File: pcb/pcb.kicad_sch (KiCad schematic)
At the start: 17 parts, among them CN10 1x2, CN2 1x8, CN3 1x8, CN4 1x8, CN5 1x4, CN6 1x2, CN7 1x2, SW1 switch_3x4, SW2 switch_3x4, SW3 219-3LPST

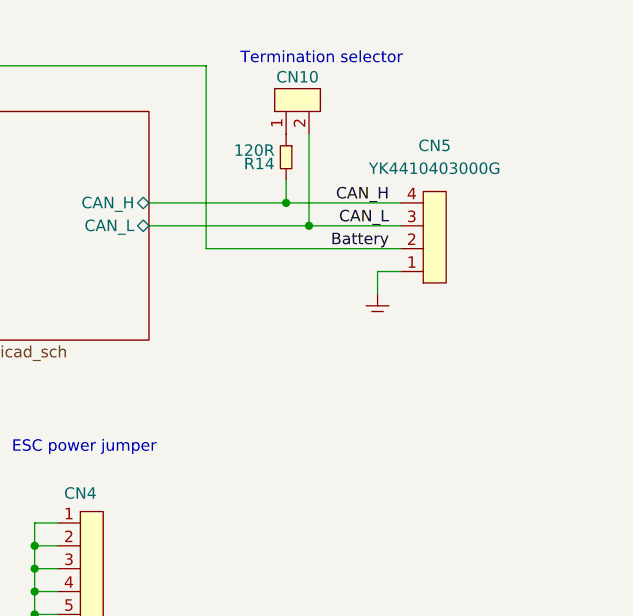
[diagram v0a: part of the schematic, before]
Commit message: changed output connector to xt60 & 2x jst-xh-4
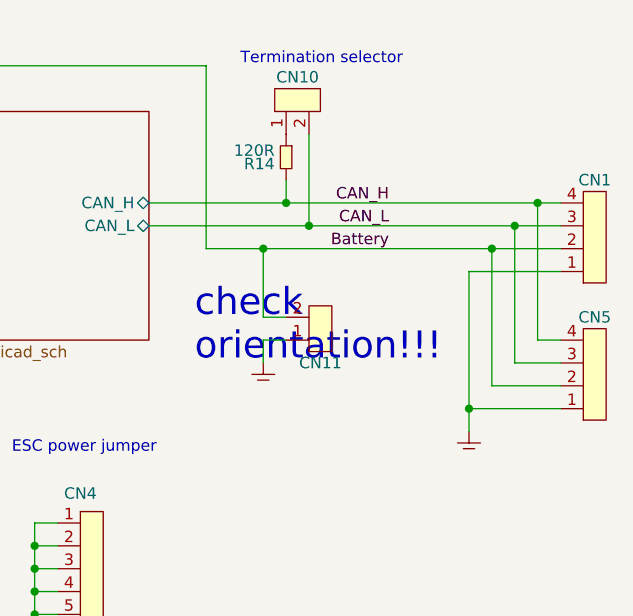
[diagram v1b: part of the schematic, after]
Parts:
- added CN1: 1x4, jst-xh:jst-xh-4, symbol jst-xh:1x4
- added CN11: 1x2, connectors:XT60, symbol pin_headers:1x2
- CN5: footprint connectors:YK4410403000G -> jst-xh:jst-xh-4; symbol pin_headers:1x4 -> jst-xh:1x4; DigiKey (none) -> 455-B4B-XH-A-ND; MPN YK4410403000G -> B4B-XH-A; Manufacturer (none) -> JST
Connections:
- net Battery: now also CN1.2, CN11.2
- net CAN_H: now also CN1.4
- net CAN_L: now also CN1.3
- net GND: now also CN1.1, CN11.1
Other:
- note added: "check orientation!!!"
- moved on the sheet: CN5

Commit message: worked on layout
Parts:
- removed CN8: ~, USB:USB4105-GF-A, symbol connectors:USB4105-GF-A
- removed R12, R13: 5k1, SMT:0603, symbol generic:R
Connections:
- net CAN_H: now also CN10.1; no longer R14.2
- net CAN_L: now also R14.2; no longer CN10.2
- net at R14.1: now also CN10.2; no longer CN10.1
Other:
- sheet MCU ports: added none; removed USB_N, USB_P
- moved on the sheet: R14

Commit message: worked on pinout
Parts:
- removed SW1, SW2: switch_3x4, buttons:sw_3x4, symbol switches:switch_3x4
- added R12: 10K, SMT:0603, symbol generic:R
- added TP1: test_point, PCB:test_point, symbol PCB:test_point
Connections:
- net GND: now also R12.1
- net MCU/DFU: now also R12.2, TP1.1 (TP)
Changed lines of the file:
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@@
     (comment 1 "User interfaces")
   )
-  (junction (at 129.54 121.92) (diameter 0) (color 0 0 0 0)
-  )
   (junction (at 251.46 109.22) (diameter 0) (color 0 0 0 0)
   )
@@
   (junction (at 203.2 132.08) (diameter 0) (color 0 0 0 0)
   )
+  (junction (at 129.54 116.84) (diameter 0) (color 0 0 0 0)
+  )
   (junction (at 129.54 137.16) (diameter 0) (color 0 0 0 0)
   )
   (junction (at 203.2 129.54) (diameter 0) (color 0 0 0 0)
   )
-  (junction (at 129.54 132.08) (diameter 0) (color 0 0 0 0)
-  )
   (junction (at 190.5 124.46) (diameter 0) (color 0 0 0 0)
   )
@@
     (stroke (width 0) (type default))
   )
-  (wire (pts (xy 129.54 116.84) (xy 132.08 116.84))
-    (stroke (width 0) (type default))
-  )
-  (wire (pts (xy 129.54 132.08) (xy 129.54 121.92))
-    (stroke (width 0) (type default))
-  )
   (wire (pts (xy 203.2 137.16) (xy 205.74 137.16))
     (stroke (width 0) (type default))
   )
+  (wire (pts (xy 129.54 116.84) (xy 129.54 119.38))
+    (stroke (width 0) (type default))
+  )
   (wire (pts (xy 203.2 127) (xy 205.74 127))
     (stroke (width 0) (type default))
@@
     (stroke (width 0) (type default))
   )
-  (wire (pts (xy 137.16 116.84) (xy 139.7 116.84))
-    (stroke (width 0) (type default))
-  )
   (wire (pts (xy 137.16 132.08) (xy 139.7 132.08))
     (stroke (width 0) (type default))
@@
     (stroke (width 0) (type default))
   )
+  (wire (pts (xy 139.7 116.84) (xy 129.54 116.84))
+    (stroke (width 0) (type default))
+  )
   (wire (pts (xy 231.14 99.06) (xy 228.6 99.06))
     (stroke (width 0) (type default))
@@
     (stroke (width 0) (type default))
   )
-  (wire (pts (xy 129.54 121.92) (xy 132.08 121.92))
-    (stroke (width 0) (type default))
-  )
   (wire (pts (xy 203.2 127) (xy 203.2 124.46))
     (stroke (width 0) (type default))
   )
-  (wire (pts (xy 137.16 121.92) (xy 139.7 121.92))
-    (stroke (width 0) (type default))
-  )
   (wire (pts (xy 193.04 114.3) (xy 190.5 114.3))
     (stroke (width 0) (type default))
@@
     (stroke (width 0) (type default))
   )
+  (wire (pts (xy 129.54 124.46) (xy 129.54 127))
+    (stroke (width 0) (type default))
+  )
   (wire (pts (xy 233.68 83.82) (xy 233.68 88.9))
     (stroke (width 0) (type default))
@@
   )
   (wire (pts (xy 256.54 88.9) (xy 261.62 88.9))
-    (stroke (width 0) (type default))
-  )
-  (wire (pts (xy 129.54 121.92) (xy 129.54 116.84))
     (stroke (width 0) (type default))
   )
@@
     )
   )
-  (symbol (lib_id "switches:switch_3x4") (at 134.62 116.84 0) (unit 1)
+  (symbol (lib_id "generic:GND") (at 129.54 127 0) (unit 1)
     (in_bom yes) (on_board yes) (dnp no) (fields_autoplaced)
-    (property "Reference" "SW1" (at 134.62 114.3 0)
-      (effects (font (size 1.27 1.27)))
-    )
-    (property "Value" "switch_3x4" (at 134.62 114.3 0)
-      (effects (font (size 1.27 1.27)) hide)
-    )
-    (property "Footprint" "buttons:sw_3x4" (at 134.62 118.11 0)
-      (effects (font (size 1.27 1.27)) hide)
-    )
-    (property "Datasheet" "" (at 134.62 116.84 0)
-      (effects (font (size 1.27 1.27)) hide)
-    )
-    (pin "1")
-    (pin "2")
-    (pin "3")
-    (pin "4")
-    (instances
-      (project "pcb"
-        (path "/6bb3bad6-1a89-4624-b34d-6ddda7dd16d2"
-          (reference "SW1") (unit 1)
+    (property "Reference" "#GND02" (at 133.35 125.73 0)
+      (effects (font (size 1.27 1.27)) hide)
+    )
+    (property "Value" "GND" (at 133.35 127 0)
+      (effects (font (size 1.27 1.27)) hide)
+    )
+    (property "Footprint" "" (at 129.54 127 0)
+      (effects (font (size 1.27 1.27)) hide)
+    )
+    (property "Datasheet" "" (at 129.54 127 0)
+      (effects (font (size 1.27 1.27)) hide)
+    )
+    (pin "~")
+    (instances
+      (project "pcb"
+        (path "/6bb3bad6-1a89-4624-b34d-6ddda7dd16d2"
+          (reference "#GND02") (unit 1)
         )
       )
@@
     )
   )
-  (symbol (lib_id "switches:switch_3x4") (at 134.62 121.92 0) (unit 1)
-    (in_bom yes) (on_board yes) (dnp no)
-    (property "Reference" "SW2" (at 134.62 119.38 0)
-      (effects (font (size 1.27 1.27)))
-    )
-    (property "Value" "switch_3x4" (at 134.62 119.38 0)
-      (effects (font (size 1.27 1.27)) hide)
-    )
-    (property "Footprint" "buttons:sw_3x4" (at 134.62 123.19 0)
-      (effects (font (size 1.27 1.27)) hide)
-    )
-    (property "Datasheet" "" (at 134.62 121.92 0)
-      (effects (font (size 1.27 1.27)) hide)
-    )
-    (pin "1")
-    (pin "2")
-    (pin "3")
-    (pin "4")
-    (instances
-      (project "pcb"
-        (path "/6bb3bad6-1a89-4624-b34d-6ddda7dd16d2/19469851-aeaf-466c-9786-c0d0ae531cf4"
-          (reference "SW2") (unit 1)
-        )
-        (path "/6bb3bad6-1a89-4624-b34d-6ddda7dd16d2"
-          (reference "SW2") (unit 1)
-        )
-      )
-    )
-  )
   (symbol (lib_id "generic:GND") (at 129.54 139.7 0) (unit 1)
     (in_bom yes) (on_board yes) (dnp no) (fields_autoplaced)
@@
     )
   )
+  (symbol (lib_id "PCB:test_point") (at 129.54 116.84 0) (mirror y) (unit 1)
+    (in_bom yes) (on_board yes) (dnp no)
+    (property "Reference" "TP1" (at 127 115.57 0)
+      (effects (font (size 1.27 1.27)) (justify left))
+    )
+    (property "Value" "test_point" (at 129.54 114.3 0)
+      (effects (font (size 1.27 1.27)) hide)
+    )
+    (property "Footprint" "PCB:test_point" (at 127 118.11 0)
+      (effects (font (size 1.27 1.27)) hide)
+    )
+    (property "Datasheet" "" (at 129.54 116.84 0)
+      (effects (font (size 1.27 1.27)) hide)
+    )
+    (pin "1")
+    (instances
+      (project "pcb"
+        (path "/6bb3bad6-1a89-4624-b34d-6ddda7dd16d2"
+          (reference "TP1") (unit 1)
+        )
+      )
+    )
+  )
   (symbol (lib_id "pin_headers:1x2") (at 60.96 78.74 0) (mirror y) (unit 1)
     (in_bom yes) (on_board yes) (dnp no) (fields_autoplaced)
@@
         )
       )
+    )
+  )
+  (symbol (lib_name "R_1") (lib_id "generic:R") (at 129.54 121.92 270) (mirror x) (unit 1)
+    (in_bom yes) (on_board yes) (dnp no)
+    (property "Reference" "R12" (at 128.27 120.65 90)
+      (effects (font (size 1.27 1.27)) (justify right))
+    )
+    (property "Value" "10K" (at 128.27 123.19 90)
+      (effects (font (size 1.27 1.27)) (justify right))
+    )
+    (property "Footprint" "SMT:0603" (at 128.905 124.46 0)
+      (effects (font (size 1.27 1.27)) hide)
+    )
+    (property "Datasheet" "" (at 129.54 121.92 0)
+      (effects (font (size 1.27 1.27)) hide)
+    )
+    (pin "1")
+    (pin "2")
+    (instances
+      (project "pcb"
+        (path "/6bb3bad6-1a89-4624-b34d-6ddda7dd16d2"
+          (reference "R12") (unit 1)
+        )
+      )

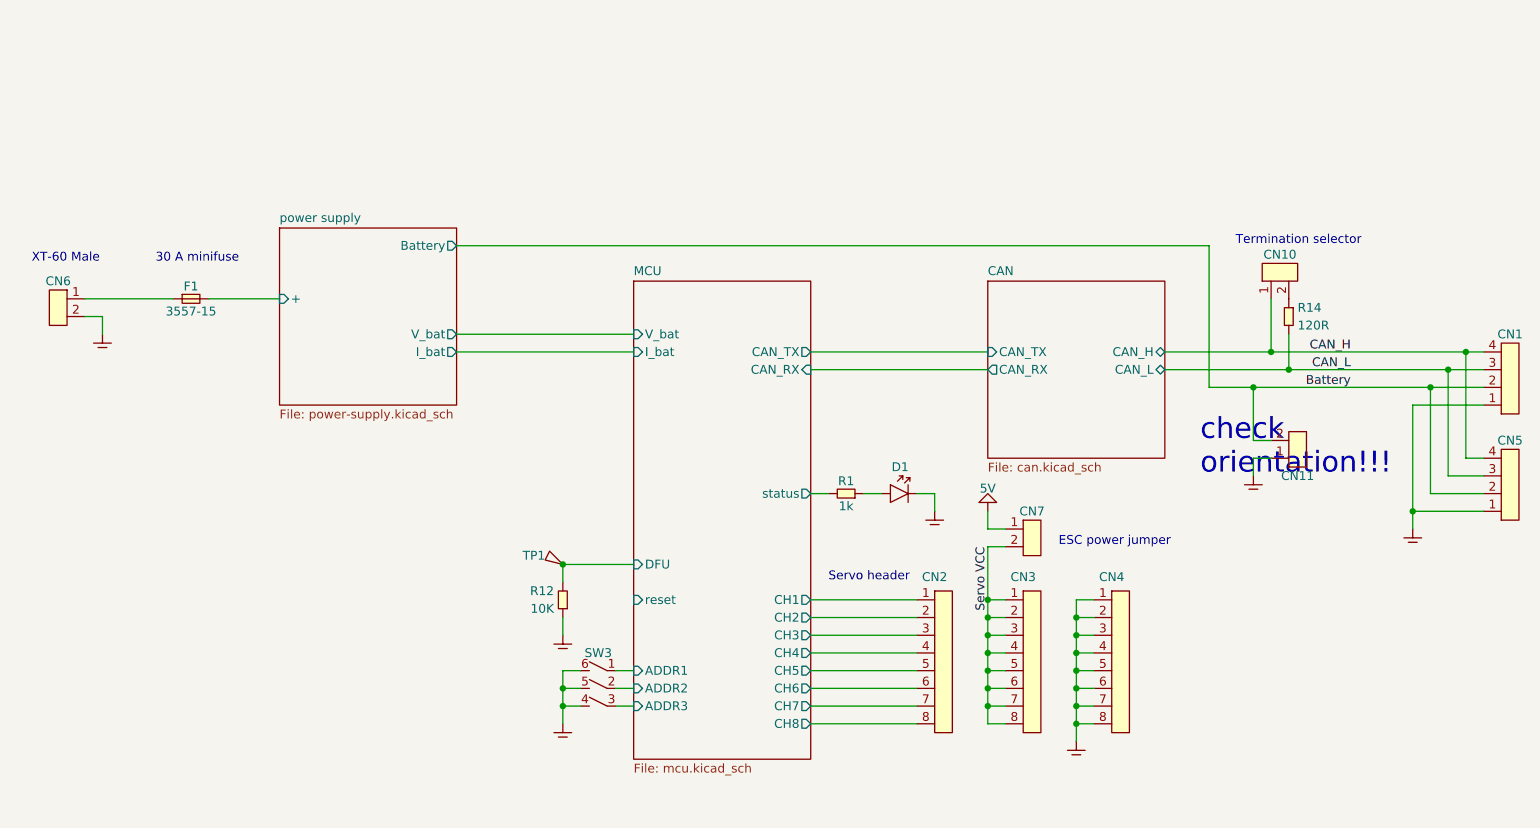
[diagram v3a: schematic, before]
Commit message: added hierarchial sheets for buffering
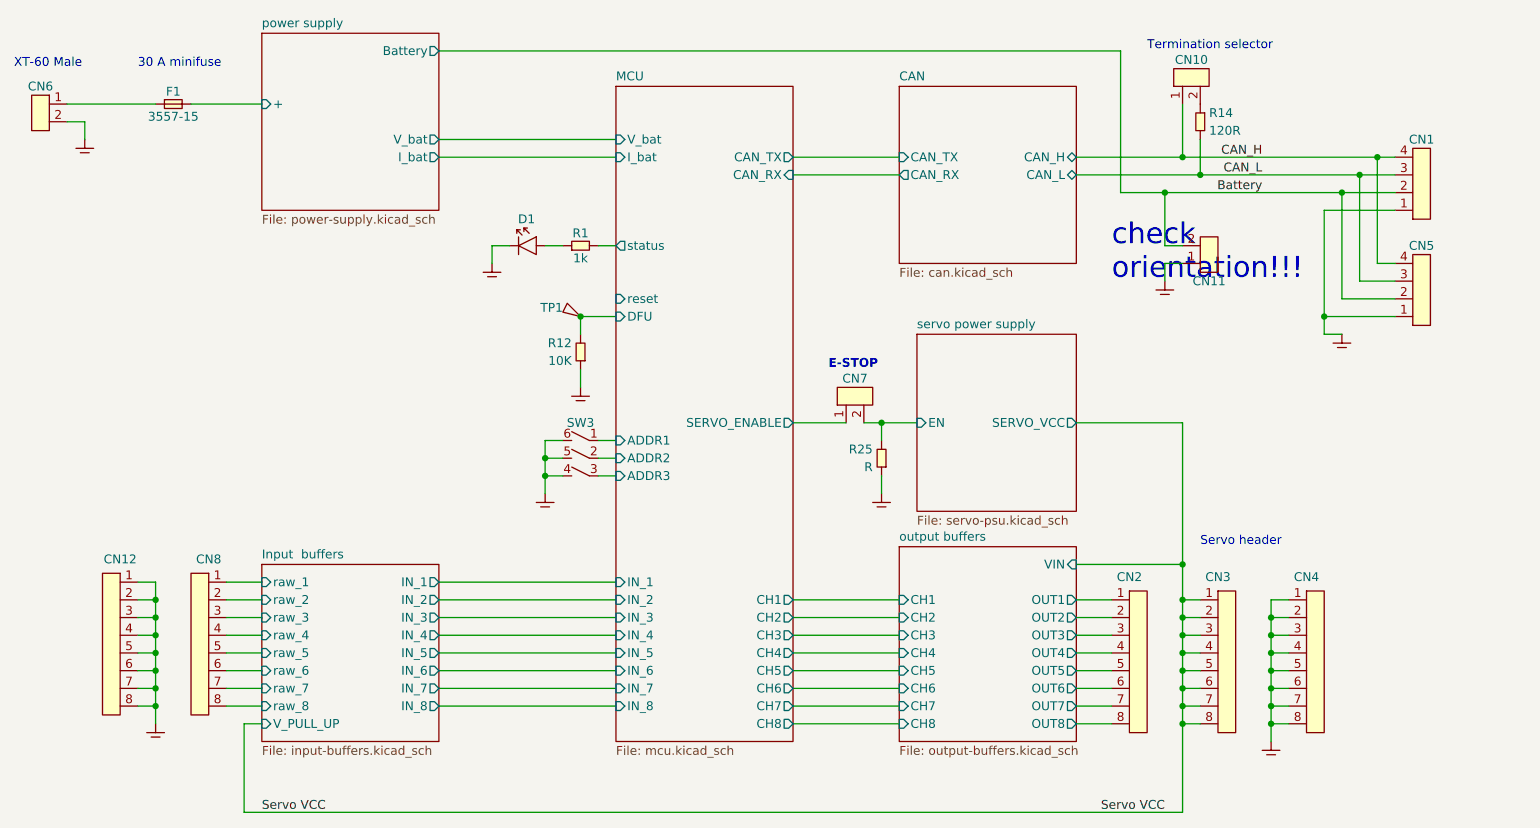
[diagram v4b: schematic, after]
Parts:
- added CN12, CN8: 1x8, pin_headers:1x8, symbol pin_headers:1x8
- added R25: R, SMT:0603, symbol generic:R
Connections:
- net GND: now also CN12.1, CN12.2, CN12.3, CN12.4, CN12.5, CN12.6, CN12.7, CN12.8, R25.1
- net MCU/CH1: no longer CN2.1
- net MCU/CH2: no longer CN2.2
- net MCU/CH3: no longer CN2.3
- net MCU/CH4: no longer CN2.4
- net MCU/CH5: no longer CN2.5
- net MCU/CH6: no longer CN2.6
- net MCU/CH7: no longer CN2.7
- net MCU/CH8: no longer CN2.8
- net Servo VCC: no longer CN7.2
- net 5V renamed MCU/SERVO_ENABLE
- new net Input  buffers/raw_1: CN8.1
- new net Input  buffers/raw_2: CN8.2
- new net Input  buffers/raw_3: CN8.3
- new net Input  buffers/raw_4: CN8.4
- new net Input  buffers/raw_5: CN8.5
- new net Input  buffers/raw_6: CN8.6
- new net Input  buffers/raw_7: CN8.7
- new net Input  buffers/raw_8: CN8.8
- new net output buffers/OUT1: CN2.1
- new net output buffers/OUT2: CN2.2
- new net output buffers/OUT3: CN2.3
- new net output buffers/OUT4: CN2.4
- new net output buffers/OUT5: CN2.5
- new net output buffers/OUT6: CN2.6
- new net output buffers/OUT7: CN2.7
- new net output buffers/OUT8: CN2.8
- new net servo power supply/EN: CN7.2, R25.2
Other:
- added sheet Input  buffers (input-buffers.kicad_sch)
- added sheet output buffers (output-buffers.kicad_sch)
- added sheet servo power supply (servo-psu.kicad_sch)
- sheet MCU ports: added IN_1, IN_2, IN_3, IN_4, IN_5, IN_6, IN_7, IN_8, SERVO_ENABLE; removed none
- note added: "E-STOP"
- note removed: "ESC power jumper"
- moved on the sheet: CN1, CN10, CN11, CN2, CN3, CN4, CN5, CN6, CN7, D1, F1, R1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

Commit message: worked on layout
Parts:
- renumbered R1 to R4
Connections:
- net output buffers/OUT1 renamed output buffers/OUT_1
- net output buffers/OUT2 renamed output buffers/OUT_2
- net output buffers/OUT3 renamed output buffers/OUT_3
- net output buffers/OUT4 renamed output buffers/OUT_4
- net output buffers/OUT5 renamed output buffers/OUT_5
- net output buffers/OUT6 renamed output buffers/OUT_6
- net output buffers/OUT7 renamed output buffers/OUT_7
- net output buffers/OUT8 renamed output buffers/OUT_8
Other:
- sheet output buffers ports: added OUT_1, OUT_2, OUT_3, OUT_4, OUT_5, OUT_6, OUT_7, OUT_8; removed OUT1, OUT2, OUT3, OUT4, OUT5, OUT6, OUT7, OUT8

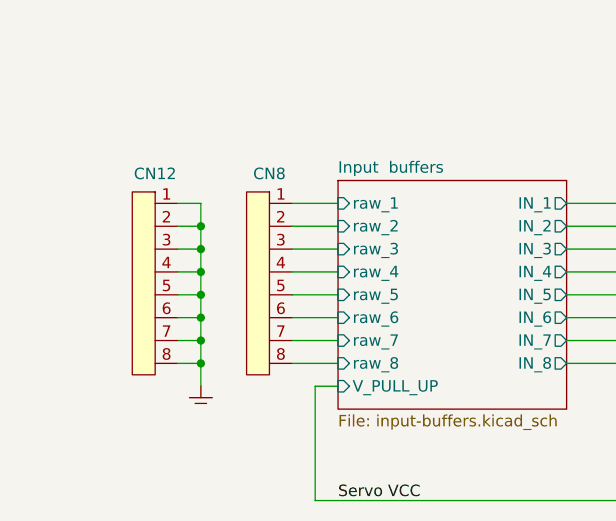
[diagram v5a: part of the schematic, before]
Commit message: fixed reversed sensor signals
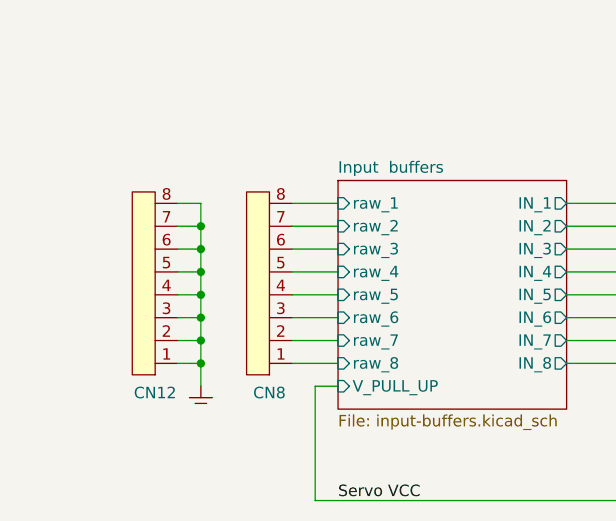
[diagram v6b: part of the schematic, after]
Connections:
- net Input  buffers/raw_1: now also CN8.8; no longer CN8.1
- net Input  buffers/raw_2: now also CN8.7; no longer CN8.2
- net Input  buffers/raw_3: now also CN8.6; no longer CN8.3
- net Input  buffers/raw_4: now also CN8.5; no longer CN8.4
- net Input  buffers/raw_5: now also CN8.4; no longer CN8.5
- net Input  buffers/raw_6: now also CN8.3; no longer CN8.6
- net Input  buffers/raw_7: now also CN8.2; no longer CN8.7
- net Input  buffers/raw_8: now also CN8.1; no longer CN8.8
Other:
- moved on the sheet: CN12, CN8
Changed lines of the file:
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@@
 	(symbol
 		(lib_id "pin_headers:1x8")
-		(at 81.28 127 0)
-		(mirror y)
+		(at 81.28 129.54 180)
 		(unit 1)
 		(exclude_from_sim no)
@@
 		(dnp no)
 		(property "Reference" "CN8"
-			(at 78.74 116.84 0)
+			(at 78.74 139.7 0)
 			(effects
 				(font
@@
 		)
 		(property "Value" "1x8"
-			(at 81.28 116.84 0)
+			(at 81.28 139.7 0)
 			(effects
 				(font
@@
 		)
 		(property "Footprint" "pin_headers:1x8"
-			(at 81.28 119.38 0)
-			(effects
-				(font
-					(size 1.27 1.27)
-				)
-				(hide yes)
-			)
-		)
-		(property "Datasheet" ""
-			(at 81.28 124.46 0)
-			(effects
-				(font
-					(size 1.27 1.27)
-				)
-				(hide yes)
-			)
-		)
-		(property "Description" ""
-			(at 81.28 127 0)
+			(at 81.28 137.16 0)
+			(effects
+				(font
+					(size 1.27 1.27)
+				)
+				(hide yes)
+			)
+		)
+		(property "Datasheet" ""
+			(at 81.28 132.08 0)
+			(effects
+				(font
+					(size 1.27 1.27)
+				)
+				(hide yes)
+			)
+		)
+		(property "Description" ""
+			(at 81.28 129.54 0)
 			(effects
 				(font
@@
 	(symbol
 		(lib_id "pin_headers:1x8")
-		(at 68.58 127 0)
-		(mirror y)
+		(at 68.58 129.54 180)
 		(unit 1)
 		(exclude_from_sim no)
@@
 		(dnp no)
 		(property "Reference" "CN12"
-			(at 66.04 116.84 0)
+			(at 66.04 139.7 0)
 			(effects
 				(font
@@
 		)
 		(property "Value" "1x8"
-			(at 68.58 116.84 0)
+			(at 68.58 139.7 0)
 			(effects
 				(font
@@
 		)
 		(property "Footprint" "pin_headers:1x8"
-			(at 68.58 119.38 0)
-			(effects
-				(font
-					(size 1.27 1.27)
-				)
-				(hide yes)
-			)
-		)
-		(property "Datasheet" ""
-			(at 68.58 124.46 0)
-			(effects
-				(font
-					(size 1.27 1.27)
-				)
-				(hide yes)
-			)
-		)
-		(property "Description" ""
-			(at 68.58 127 0)
-			(effects
-				(font
+			(at 68.58 137.16 0)
+			(effects
+				(font
+					(size 1.27 1.27)
+				)
+				(hide yes)
+			)
+		)
+		(property "Datasheet" ""
+			(at 68.58 132.08 0)
+			(effects
+				(font
+					(size 1.27 1.27)
+				)
+				(hide yes)
+			)
+		)
+		(property "Description" ""
+			(at 68.58 129.54 0)
+			(effects
+				(font
